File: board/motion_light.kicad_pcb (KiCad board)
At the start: 2 copper layers, 35 x 64 mm, 20 parts, among them CON1 AVR-ISP-6, J1 MOTION (optional), J2 GPIO, SW1 SW_Push, SW2 SW_Push, U1 ATTINY84A-SSU, U2 APA102, U3 APA102, U4 PIR_MODULE

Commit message: Fix PIR orientation; update PIR silk; add more silk labels
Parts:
- R4: value 66.5K -> 68K
- turned U4 to 90 degrees
- renumbered J2 to GPIO, CON1 to ISP, J1 to J2
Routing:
- net /BUTTON2: track 35.8 -> 37.1 mm
- net /MOTION: track 48.2 -> 49.4 mm
- net GND: track 14.7 -> 15.4 mm
- net VCC: track 0.53 -> 0.00 mm
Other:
- board text added: "MOT"
- board text added: "Motion Night Light 2017 Steve Pomeroy staticfree.info Version 1.0.0"
- board text removed: "Motion Night Light 2017 Steve Pomeroy staticfree.info Version 0.5"
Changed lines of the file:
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@@
     (links 40)
     (no_connects 0)
-    (area 84.150001 53.05 202.15 137.151426)
+    (area 113.924999 59.924999 149.075001 124.075001)
     (thickness 1.6)
-    (drawings 20)
-    (tracks 136)
+    (drawings 26)
+    (tracks 139)
     (zones 0)
     (modules 20)
@@
       (effects (font (size 1 1) (thickness 0.15)))
     )
-    (fp_text value 10K (at -2.9 -0.4 360) (layer F.Fab)
-      (effects (font (size 1 1) (thickness 0.15)))
+    (fp_text value 10K (at 0.1 0 360) (layer F.SilkS)
+      (effects (font (size 0.7 0.7) (thickness 0.1)))
     )
     (fp_text user %R (at 0 0 270) (layer F.Fab)
@@
     (tags "resistor 0805")
     (attr smd)
-    (fp_text reference R4 (at 0 1.7 180) (layer F.SilkS)
-      (effects (font (size 1 1) (thickness 0.15)))
-    )
-    (fp_text value 66.5K (at 0 1.75 180) (layer F.Fab)
-      (effects (font (size 1 1) (thickness 0.15)))
+    (fp_text reference R4 (at -0.05 1.8 180) (layer F.SilkS)
+      (effects (font (size 1 1) (thickness 0.15)))
+    )
+    (fp_text value 68K (at -0.05 0 270) (layer F.SilkS)
+      (effects (font (size 0.7 0.7) (thickness 0.1)))
     )
     (fp_text user %R (at 0 0 180) (layer F.Fab)
@@
     (descr "Resistor, LDR 5.1x3.4mm")
     (tags "Resistor LDR5.1x3.4mm")
-    (fp_text reference R1 (at 1.7 -2.9 90) (layer F.SilkS)
+    (fp_text reference R1 (at 5.8 -0.1 90) (layer F.SilkS)
       (effects (font (size 1 1) (thickness 0.15)))
     )
@@
     (descr "Through hole straight pin header, 1x05, 2.54mm pitch, single row")
     (tags "Through hole pin header THT 1x05 2.54mm single row")
-    (fp_text reference J2 (at 0 -2.33 270) (layer F.SilkS)
+    (fp_text reference GPIO (at 0 -2.33 270) (layer F.SilkS)
       (effects (font (size 1 1) (thickness 0.15)))
     )
@@
     (descr "Through hole straight pin header, 2x03, 2.54mm pitch, double rows")
     (tags "Through hole pin header THT 2x03 2.54mm double row")
-    (fp_text reference CON1 (at 1.27 -2.39 90) (layer F.SilkS)
+    (fp_text reference ISP (at 1.27 -2.39 90) (layer F.SilkS)
       (effects (font (size 1 1) (thickness 0.15)))
     )
@@
     (descr "Through hole angled pin header, 1x03, 2.54mm pitch, 6mm pin length, single row")
     (tags "Through hole angled pin header THT 1x03 2.54mm single row")
-    (fp_text reference J1 (at -2.4 -0.8) (layer F.SilkS)
+    (fp_text reference J2 (at 0 -2.4) (layer F.SilkS)
       (effects (font (size 1 1) (thickness 0.15)))
     )
@@
     (tags "resistor 0805")
     (attr smd)
-    (fp_text reference D1 (at 3.1 0.05 180) (layer F.SilkS)
+    (fp_text reference D1 (at 3.2 0.05 270) (layer F.SilkS)
       (effects (font (size 1 1) (thickness 0.15)))
     )
@@
     (tags "resistor 0805")
     (attr smd)
-    (fp_text reference R3 (at 3 0 180) (layer F.SilkS)
-      (effects (font (size 1 1) (thickness 0.15)))
-    )
-    (fp_text value 1K (at 0 1.75 90) (layer F.Fab)
-      (effects (font (size 1 1) (thickness 0.15)))
+    (fp_text reference R3 (at -3.3 -0.8 270) (layer F.SilkS)
+      (effects (font (size 1 1) (thickness 0.15)))
+    )
+    (fp_text value 1K (at -0.1 0 180) (layer F.SilkS)
+      (effects (font (size 0.7 0.7) (thickness 0.1)))
     )
     (fp_text user %R (at 0 0 90) (layer F.Fab)
@@
     (descr "tactile switch SPST right angle, PTS645VL83-2 LFS")
     (tags "tactile switch SPST angled PTS645VL83-2 LFS C&K Button")
-    (fp_text reference SW1 (at 2.25 1.68 90) (layer F.SilkS)
+    (fp_text reference SW1 (at 2.2 1.8 90) (layer F.SilkS)
       (effects (font (size 1 1) (thickness 0.15)))
     )
@@
     (descr "tactile switch SPST right angle, PTS645VL83-2 LFS")
     (tags "tactile switch SPST angled PTS645VL83-2 LFS C&K Button")
-    (fp_text reference SW2 (at 2.25 1.68 90) (layer F.SilkS)
+    (fp_text reference SW2 (at 2.3 1.8 90) (layer F.SilkS)
       (effects (font (size 1 1) (thickness 0.15)))
     )
@@
   )
   (module StaticfreeFootprints:PaPIR_PIR_SENSOR (layer F.Cu)
-    (at 126.5 92 180)
-    (fp_text reference U4 (at 0 -7.7 180) (layer F.SilkS)
-      (effects (font (size 1 1) (thickness 0.15)))
-    )
-    (fp_text value PIR_MODULE (at -2.1 -6.8 180) (layer F.Fab)
+    (at 126.5 92 90)
+    (fp_text reference U4 (at -0.2 6.9 90) (layer F.SilkS)
+      (effects (font (size 1 1) (thickness 0.15)))
+    )
+    (fp_text value PIR_MODULE (at -2.1 -6.8 90) (layer F.Fab)
       (effects (font (size 1 1) (thickness 0.15)))
     )
     (fp_circle (center 0 0) (end 5.5 0) (layer F.Fab) (width 0.15))
-    (fp_line (start -0.254 -6.604) (end -0.254 -5.9944) (layer F.SilkS) (width 0.15))
-    (fp_line (start 0.254 -6.604) (end -0.254 -6.604) (layer F.SilkS) (width 0.15))
-    (fp_line (start 0.254 -5.9944) (end 0.254 -6.604) (layer F.SilkS) (width 0.15))
+    (fp_line (start -6.604 0.254) (end -5.9944 0.254) (layer F.SilkS) (width 0.15))
+    (fp_line (start -6.604 -0.254) (end -6.604 0.254) (layer F.SilkS) (width 0.15))
+    (fp_line (start -5.9944 -0.254) (end -6.604 -0.254) (layer F.SilkS) (width 0.15))
     (fp_circle (center 0 0) (end 6 0) (layer F.SilkS) (width 0.15))
-    (pad 3 thru_hole circle (at 1.778 -1.778 180) (size 1.524 1.524) (drill 0.762) (layers *.Cu *.Mask)
+    (pad 3 thru_hole circle (at 1.778 -1.778 90) (size 1.524 1.524) (drill 0.762) (layers *.Cu *.Mask)
       (net 5 GND))
-    (pad 2 thru_hole circle (at 1.778 1.778 180) (size 1.524 1.524) (drill 0.762) (layers *.Cu *.Mask)
+    (pad 2 thru_hole circle (at 1.778 1.778 90) (size 1.524 1.524) (drill 0.762) (layers *.Cu *.Mask)
       (net 6 /MOTION))
-    (pad 1 thru_hole rect (at -1.778 1.778 180) (size 1.524 1.524) (drill 0.762) (layers *.Cu *.Mask)
+    (pad 1 thru_hole rect (at -1.778 1.778 90) (size 1.524 1.524) (drill 0.762) (layers *.Cu *.Mask)
       (net 1 VCC))
   )
+  (gr_text MOT (at 145.6 73.3 90) (layer F.SilkS)
+    (effects (font (size 0.7 0.7) (thickness 0.1)))
+  )
+  (gr_text VCC (at 145.6 70.7 90) (layer F.SilkS)
+    (effects (font (size 0.7 0.7) (thickness 0.1)))
+  )
+  (gr_text GND (at 145.6 68.2 90) (layer F.SilkS)
+    (effects (font (size 0.7 0.7) (thickness 0.1)))
+  )
+  (gr_line (start 119.25 92.3) (end 118.85 91.7) (layer F.SilkS) (width 0.2))
+  (gr_line (start 119.65 91.7) (end 119.25 92.3) (layer F.SilkS) (width 0.2))
+  (gr_line (start 118.85 91.7) (end 119.65 91.7) (layer F.SilkS) (width 0.2))
   (dimension 4 (width 0.3) (layer Dwgs.User)
     (gr_text "4.000 mm" (at 107.4 62 90) (layer Dwgs.User)
@@
     (arrow2b (pts (xy 104 82.75) (xy 104.586421 83.876504)))
   )
-  (gr_text "Motion Night Light\n2017 Steve Pomeroy\nstaticfree.info\nVersion 0.5" (at 131.6 116.3) (layer F.SilkS)
+  (gr_text "Motion Night Light\n2017 Steve Pomeroy\nstaticfree.info\nVersion 1.0.0" (at 131.6 116.3) (layer F.SilkS)
     (effects (font (size 1.5 1.5) (thickness 0.3)))
   )
@@
   (gr_line (start 149 60) (end 149 124) (layer Edge.Cuts) (width 0.15))
   (gr_line (start 114 60) (end 149 60) (layer Edge.Cuts) (width 0.15))
-  (segment (start 127.9 89.844) (end 128.278 90.222) (width 0.4) (layer F.Cu) (net 1) (status 30))
   (segment (start 145.6 85.5) (end 145.6 84.624264) (width 0.25) (layer F.Cu) (net 2))
   (segment (start 145.6 84.624264) (end 134.2 73.224264) (width 0.25) (layer F.Cu) (net 2))
@@
   (segment (start 126.58 70.79) (end 127.09 71.3) (width 0.4) (layer F.Cu) (net 5))
   (segment (start 127.09 71.3) (end 127.79 71.3) (width 0.4) (layer F.Cu) (net 5) (status 20))
+  (segment (start 125.2 89.744) (end 124.722 90.222) (width 0.25) (layer F.Cu) (net 5) (status 30))
+  (segment (start 128.278 90.222) (end 128.278 87.178) (width 0.25) (layer F.Cu) (net 6))
+  (segment (start 128.278 87.178) (end 125.3 84.2) (width 0.25) (layer F.Cu) (net 6))
+  (segment (start 125.3 84.2) (end 125.2 84.2) (width 0.25) (layer F.Cu) (net 6))
   (segment (start 140.9 69.1) (end 140.9 72.139002) (width 0.25) (layer F.Cu) (net 6))
   (segment (start 140.9 72.139002) (end 142.040998 73.28) (width 0.25) (layer F.Cu) (net 6))
@@
   (segment (start 125.2 84.2) (end 125.2 73.8) (width 0.25) (layer F.Cu) (net 6) (status 10))
   (segment (start 125.2 73.8) (end 125.8 73.2) (width 0.25) (layer F.Cu) (net 6))
-  (segment (start 125.2 84.2) (end 125.2 89.744) (width 0.25) (layer F.Cu) (net 6) (status 30))
-  (segment (start 125.2 89.744) (end 124.722 90.222) (width 0.25) (layer F.Cu) (net 6) (status 30))
   (segment (start 125.8 84.1) (end 125.9 84.2) (width 0.25) (layer F.Cu) (net 6) (status 30))
   (via (at 125.8 73.2) (size 0.6) (drill 0.4) (layers F.Cu B.Cu) (net 6))
@@
   (via (at 132.9 79.1) (size 0.6) (drill 0.4) (layers F.Cu B.Cu) (net 16))
   (segment (start 132.9 76.73) (end 132.87 76.7) (width 0.25) (layer F.Cu) (net 16) (status 30))
+  (segment (start 131.9 94.9) (end 124.174999 102.625001) (width 0.25) (layer B.Cu) (net 17))
+  (segment (start 124.174999 102.625001) (end 118.274999 102.625001) (width 0.25) (layer B.Cu) (net 17))
+  (segment (start 118.274999 102.625001) (end 117.4 103.5) (width 0.25) (layer B.Cu) (net 17))
+  (segment (start 131.9 92.9) (end 131.9 94.9) (width 0.25) (layer B.Cu) (net 17))
   (segment (start 131.9 81.7) (end 130.33 80.13) (width 0.25) (layer F.Cu) (net 17))
   (segment (start 130.33 80.13) (end 130.33 76.7) (width 0.25) (layer F.Cu) (net 17))
   (segment (start 131.9 92.9) (end 131.9 81.7) (width 0.25) (layer F.Cu) (net 17))
-  (segment (start 128.1 92.8) (end 131.8 92.8) (width 0.25) (layer B.Cu) (net 17))
   (segment (start 131.8 92.8) (end 131.9 92.9) (width 0.25) (layer B.Cu) (net 17))
   (via (at 131.9 92.9) (size 0.6) (drill 0.4) (layers F.Cu B.Cu) (net 17))
-  (segment (start 117.4 103.5) (end 128.1 92.8) (width 0.25) (layer B.Cu) (net 17) (status 10))
   (zone (net 5) (net_name GND) (layer B.Cu) (hatch edge 0.508)
     (connect_pads (clearance 0.508))

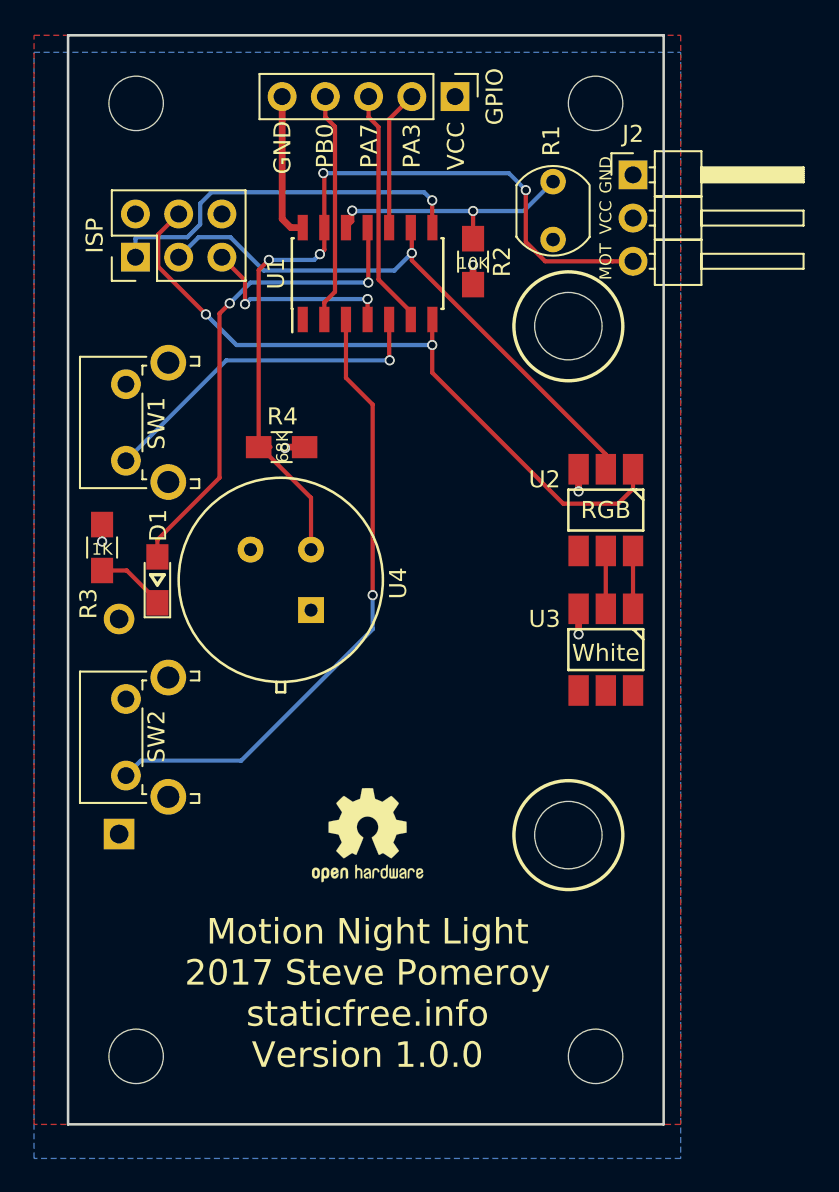
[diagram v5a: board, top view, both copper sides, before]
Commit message: Add decoupling cap
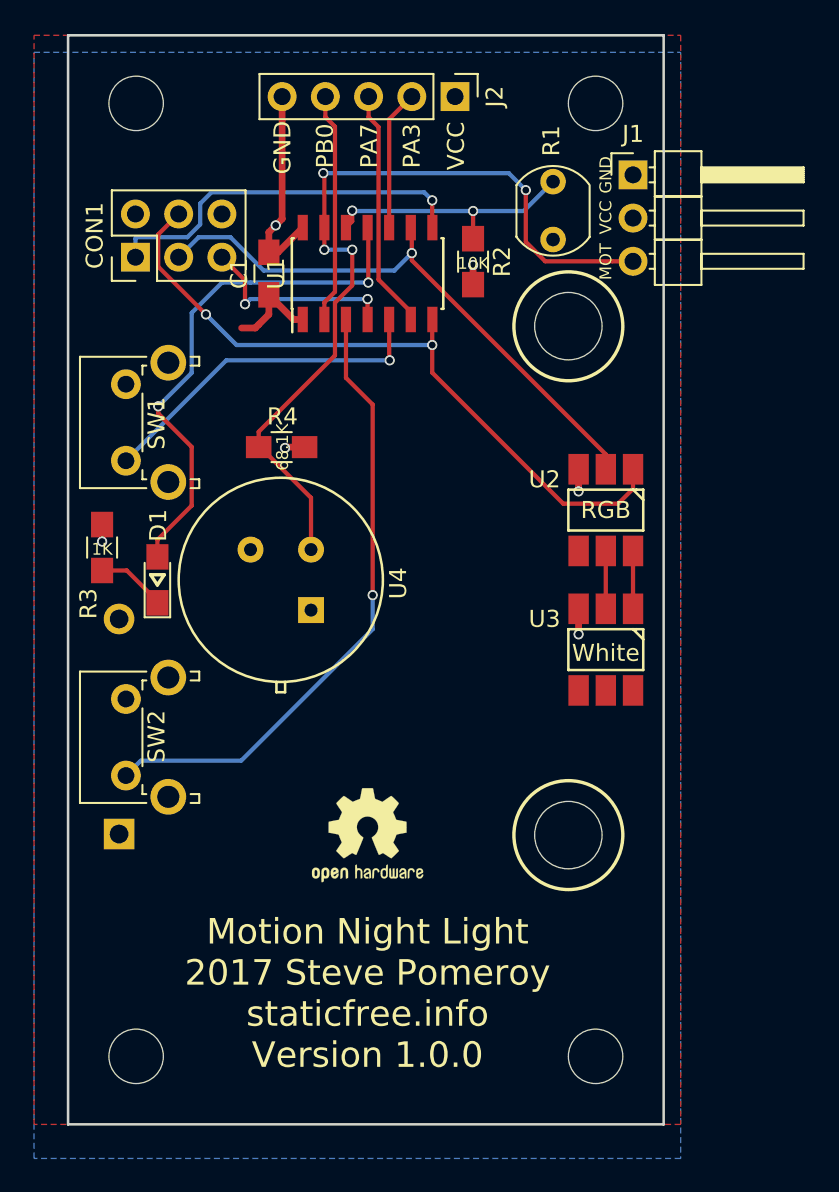
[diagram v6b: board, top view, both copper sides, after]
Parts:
- added C1: 10uF, Capacitors_SMD:C_0805_HandSoldering, F.Cu at (125.8, 74.0)
- J1: renamed from J2; value MOTION (optional) -> MOTION
- J2: renamed from GPIO; value GPIO -> Conn_01x05
- R4: value 68K -> 68.1K
- renumbered ISP to CON1
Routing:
- net VCC: track 0.00 -> 5.67 mm
- net GND: track 15.4 -> 19.0 mm, vias 5 -> 6
- net /STATUS_LED: track 28.6 -> 31.2 mm
- net /MOTION: track 49.4 -> 50.0 mm

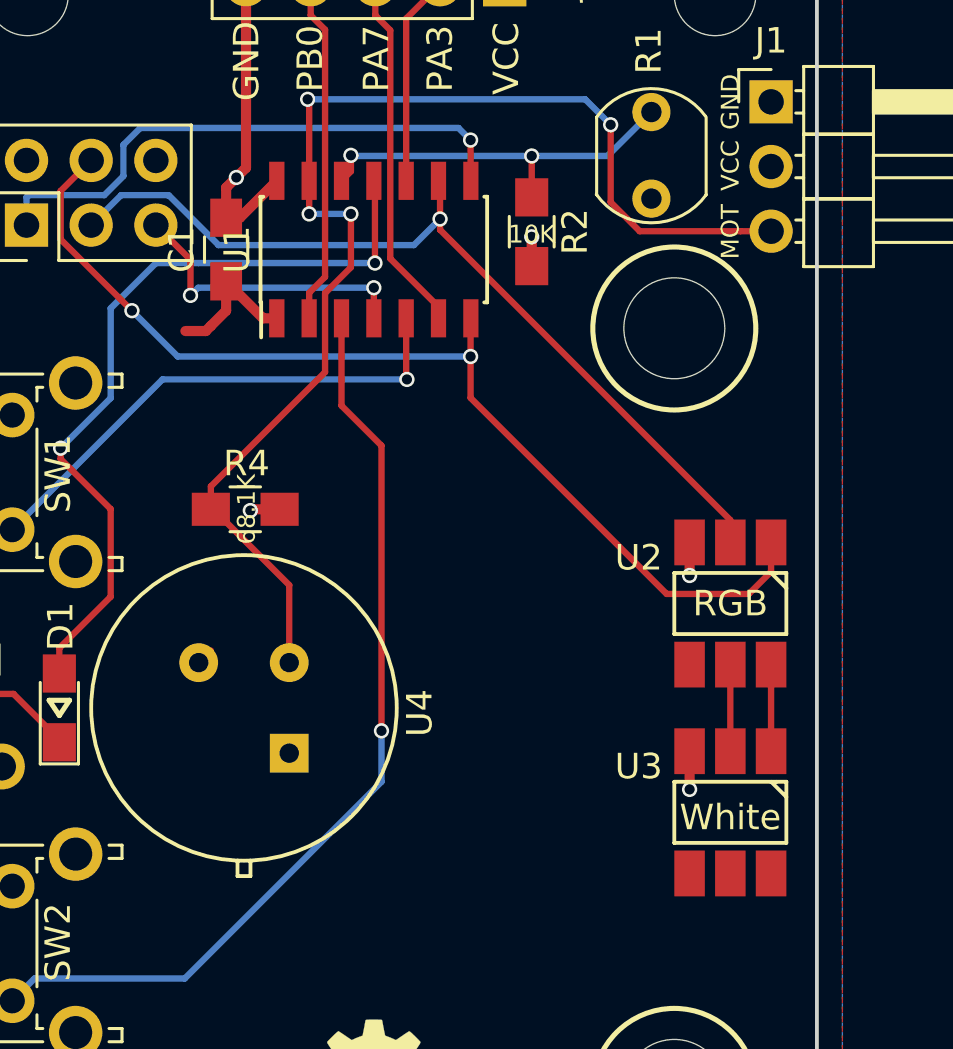
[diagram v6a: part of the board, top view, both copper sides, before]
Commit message: Rotate LEDs to make them closer together and easier to solder
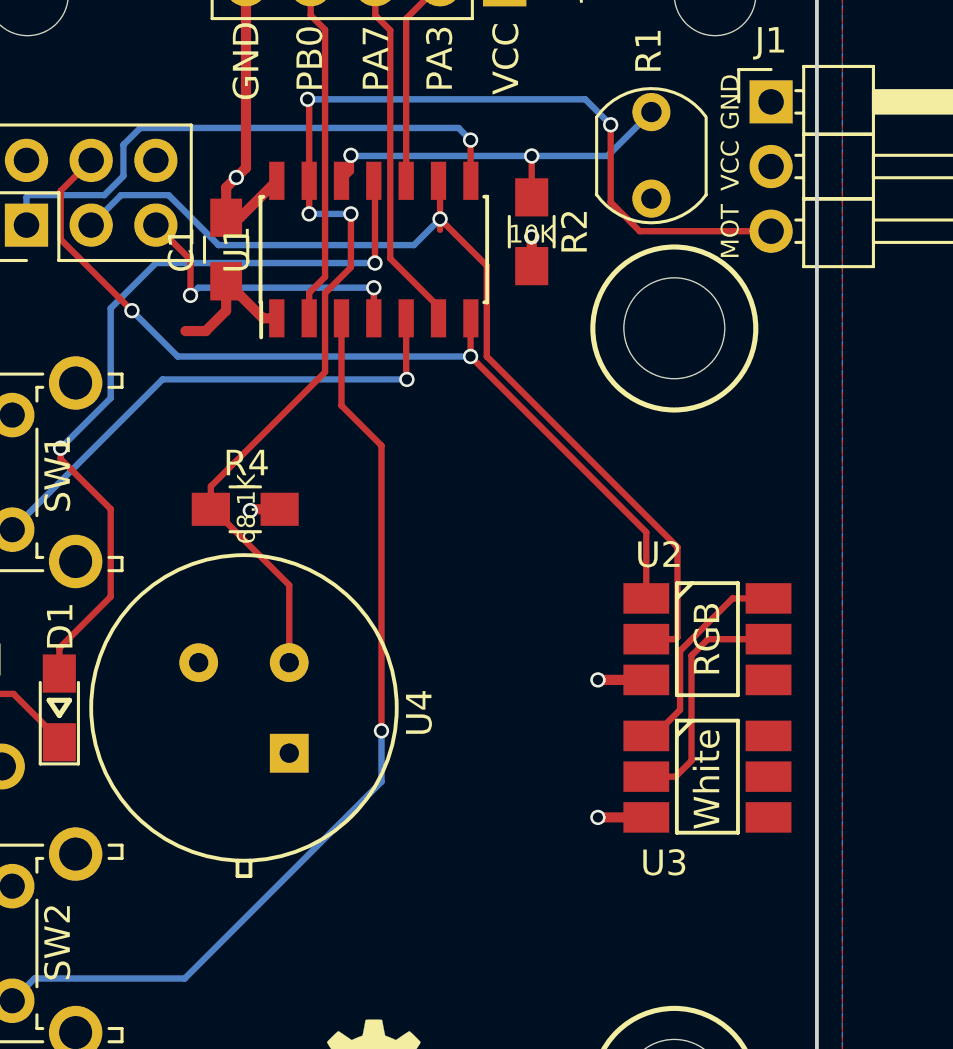
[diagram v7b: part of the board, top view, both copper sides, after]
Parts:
- moved U2 1.66 mm to (144.7, 89.3), turned to 270 degrees
- moved U3 1.66 mm to (144.7, 94.7), turned to 270 degrees
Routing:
- net Net-(U2-Pad5): track 3.40 -> 9.45 mm
- net /SDA: track 41.2 -> 35.5 mm
- net Net-(U2-Pad6): track 3.40 -> 8.39 mm
- net /SCK: track 34.4 -> 38.9 mm
- net GND: track 19.0 -> 20.0 mm

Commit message: Schematic changes of unknown variety
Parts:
- added Q1: BSS83P, TO_SOT_Packages_SMD:SOT-23, F.Cu at (145.8, 83.7)
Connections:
- J2 pad 2: /PA3 -> /ACC_PWR
- R1 pad 1: VCC -> /ACC_PWR
- U1 pad 10: /PA3 -> /~ACC_PWR_EN
- U2 pad 4: VCC -> /ACC_PWR
- U3 pad 4: VCC -> /ACC_PWR
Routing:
- net /ACC_PWR: track 0.00 -> 48.0 mm, vias 0 -> 2
- net /~ACC_PWR_EN: track 0.00 -> 17.9 mm, vias 0 -> 2
- net /PA3: track 8.25 -> 0.00 mm
- net VCC: track 5.67 -> 6.78 mm, vias 0 -> 1
